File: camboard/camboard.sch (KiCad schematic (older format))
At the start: 50 parts, among them J2 Micro_SD_Card, J3 PPTC102LFBN-RC, J4 Conn_ARM_JTAG_SWD_20, J6 Conn_02x24_Row_Letter_First, SW1 SW_DPDT_x2, SW2 SW_Push, SW3 SW_Push, SW4 SW_DPDT_x2, U1 STM32F746VGT6, U2 MCP1703A-3302_SOT23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

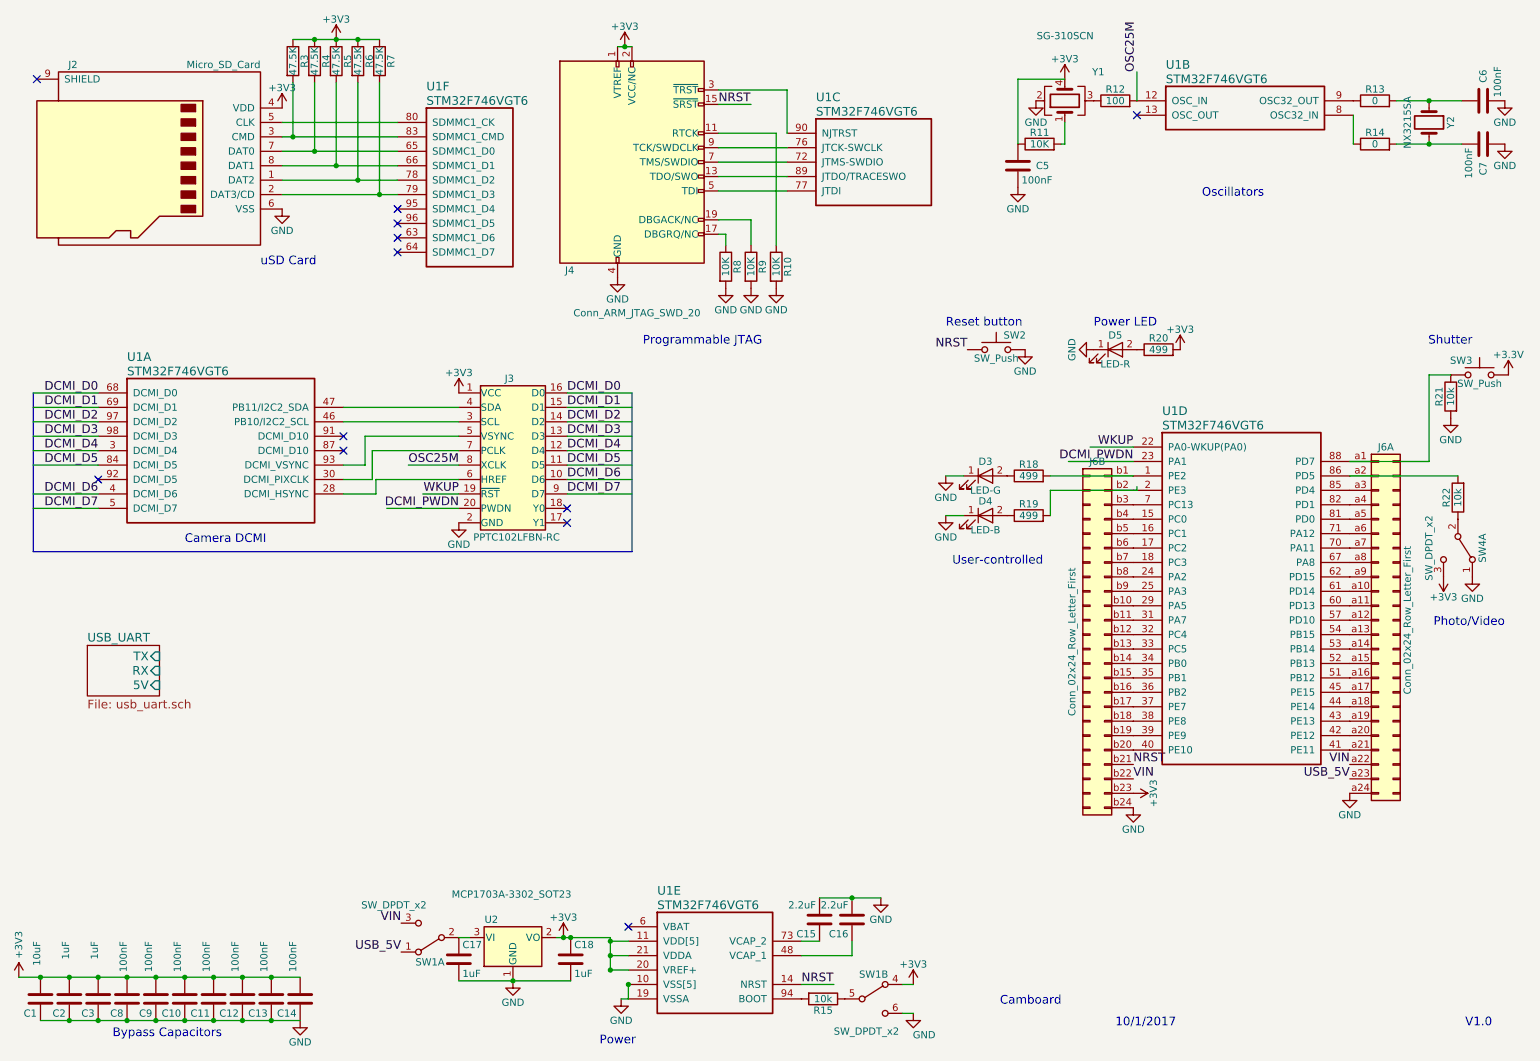
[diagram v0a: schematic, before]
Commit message: Made some more hierarchies
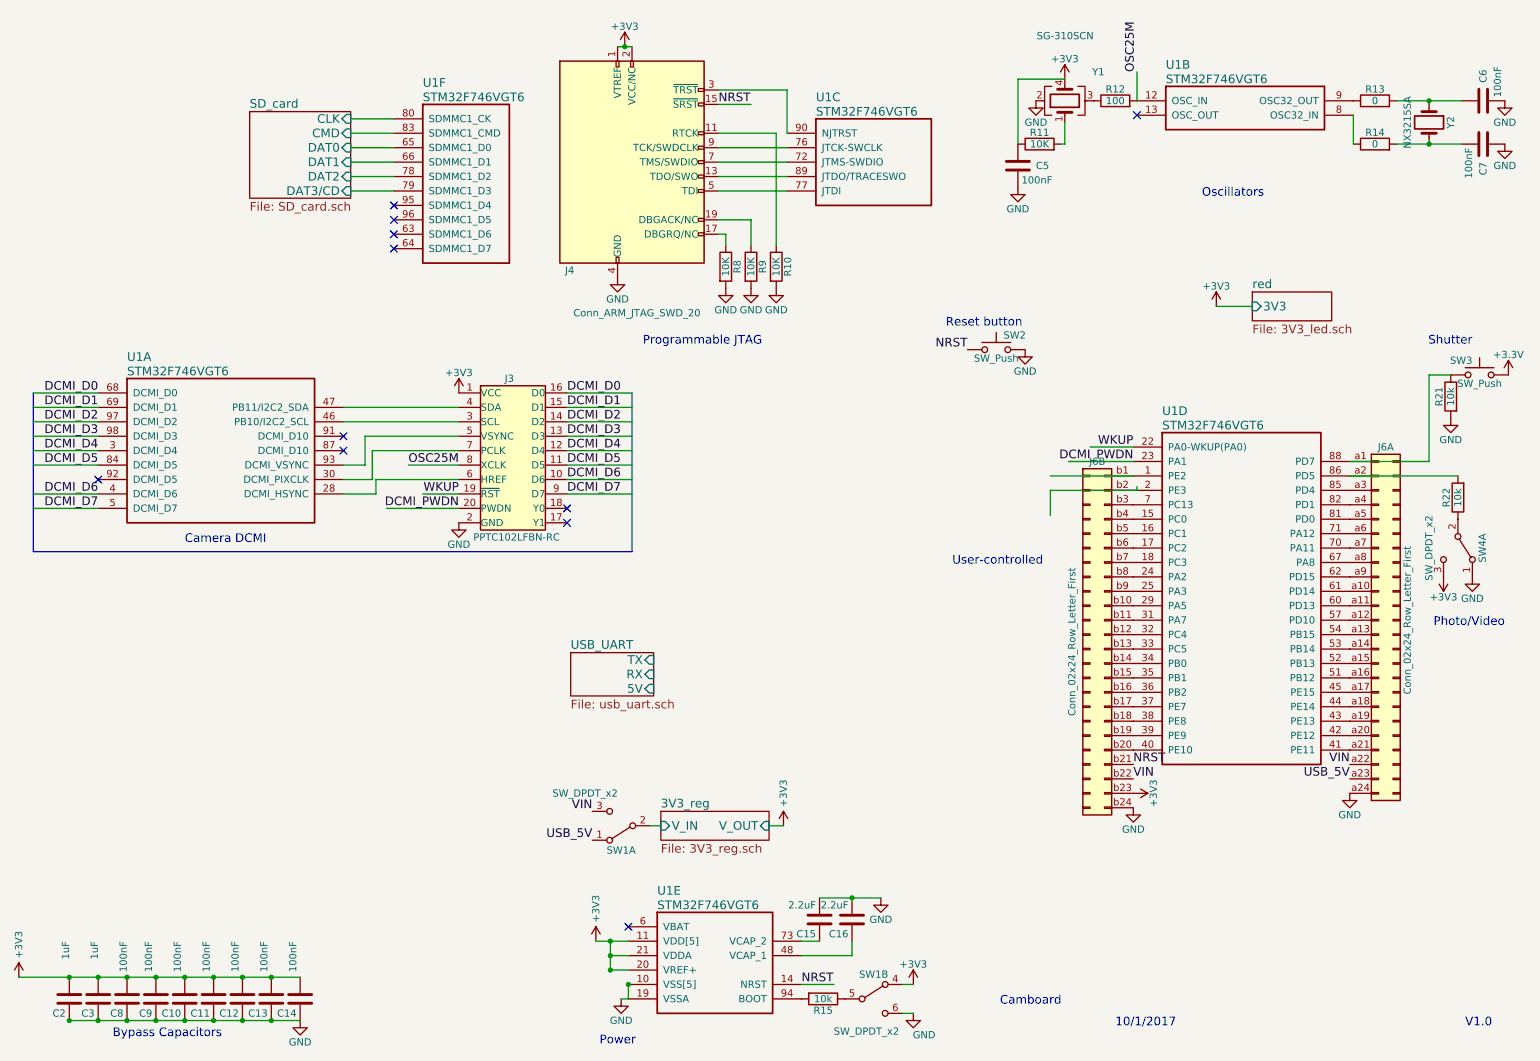
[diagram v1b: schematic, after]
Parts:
- removed C1: 10uF, Capacitors_SMD:C_0805, symbol C
- removed C17, C18: 1uF, Capacitors_SMD:C_0603, symbol C
- removed D3: LED-G, LEDs:LED_0805, symbol LED
- removed D4: LED-B, LEDs:LED_0805, symbol LED
- removed D5: LED-R, LEDs:LED_0805, symbol LED
- removed J2: Micro_SD_Card, symbol Micro_SD_Card
- removed R18, R19, R20: 499, Resistors_SMD:R_0603, symbol R
- removed R3, R4, R5, R6, R7: 47.5K, Resistors_SMD:R_0603, symbol R
- removed U2: MCP1703A-3302_SOT23, TO_SOT_Packages_SMD:SOT-23, symbol MCP1703A-3302_SOT23
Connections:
- wire segments 128 -> 86
- no-connect marks 12 -> 11
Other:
- note removed: "Power LED"
- note removed: "uSD Card"
- moved on the sheet: SW1A, U1F
